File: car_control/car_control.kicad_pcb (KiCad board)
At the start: 2 copper layers, 55.9 x 76.8 mm, 21 parts, among them J1 Conn_01x02, J2 Conn_01x03, J3 Conn_01x03, Q1 IRF540N, Q2 Q_Photo_NPN, SW1 SW_SPST

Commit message: initial schematic done?
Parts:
- added H1: MountingHole, MountingHole:MountingHole_2.7mm_M2.5_DIN965_Pad, F.Cu at (135.3, 30.5)
- added H2: MountingHole, MountingHole:MountingHole_2.7mm_M2.5_DIN965_Pad, F.Cu at (184.8, 30.5)
- added H3: MountingHole, MountingHole:MountingHole_2.7mm_M2.5_DIN965_Pad, F.Cu at (184.8, 101.0)
- added H4: MountingHole, MountingHole:MountingHole_2.7mm_M2.5_DIN965_Pad, F.Cu at (135.3, 101.0)
- SW1: footprint Connector_PinHeader_2.54mm:PinHeader_1x02_P2.54mm_Vertical -> mini_slide_switch:OS102011MA1QN1
- moved J2 11.7 mm to (157.5, 38.1)
- moved D6 8.26 mm to (142.9, 100.3)
- moved R5 8.26 mm to (142.9, 94.0)
- moved D5 6.35 mm to (141.0, 30.5)
- moved R4 6.35 mm to (141.0, 35.6)
- moved J3 4.62 mm to (157.5, 31.1)
- moved SW1 0.83 mm to (134.1, 68.6), turned to -90 degrees

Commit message: working on mechanics
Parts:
- removed BT1: Battery, Connector_PinHeader_2.54mm:PinHeader_1x02_P2.54mm_Vertical
- added J4: Screw_Terminal_01x02, Connector_Wuerth:Wuerth_WR-WTB_64800211622_1x02_P1.50mm_Vertical, F.Cu at (134.6, 44.7)
- J1: value Conn_01x02 -> Screw_Terminal_01x02; footprint Connector_PinHeader_2.54mm:PinHeader_1x02_P2.54mm_Vertical -> Connector_Wuerth:Wuerth_WR-WTB_64800211622_1x02_P1.50mm_Vertical
- moved R3 56.7 mm to (144.1, 81.9)
- moved R4 46.4 mm to (138.4, 81.9)
- moved D2 28.2 mm to (146.1, 71.1)
- moved Q1 10.8 mm to (179.1, 68.6)
- moved R6 10.5 mm to (165.1, 92.1)
- moved A1 9.85 mm to (151.1, 43.2)
- moved J1 9.44 mm to (178.4, 44.6), turned to 90 degrees
- moved R1 9.03 mm to (154.9, 92.1)
- moved R2 9.03 mm to (160.0, 92.1)
- moved D3 7.73 mm to (177.8, 84.5)
- moved Q2 7.73 mm to (177.8, 89.5)
- moved R5 7.24 mm to (149.9, 92.1)
- moved H3 6.38 mm to (178.4, 100.3)
- moved D4 6.35 mm to (168.9, 30.5)
- moved D7 6.35 mm to (168.9, 100.3)
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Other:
- board size 55.9 x 76.8 mm -> 50.8 x 76.2 mm

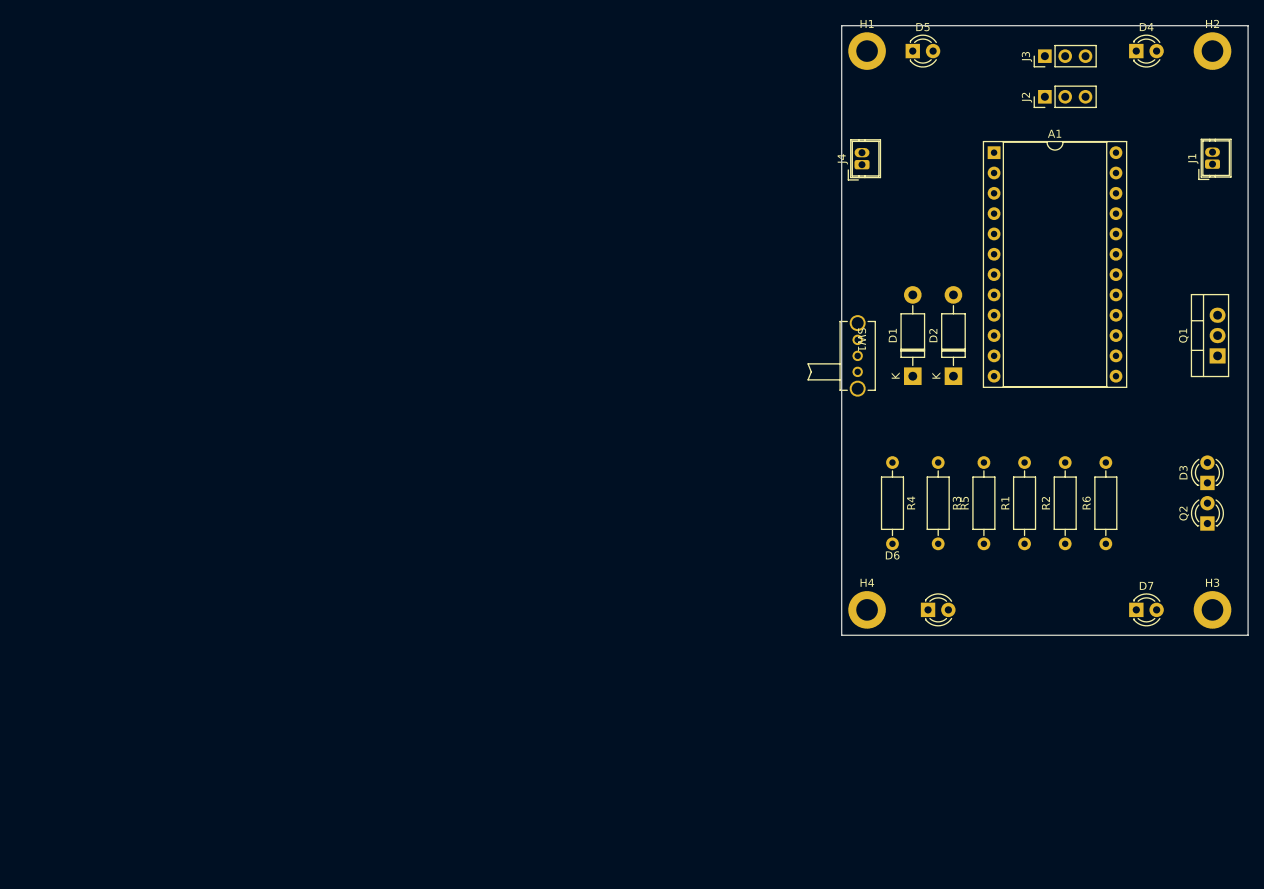
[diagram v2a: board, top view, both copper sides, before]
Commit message: New board outline with wings
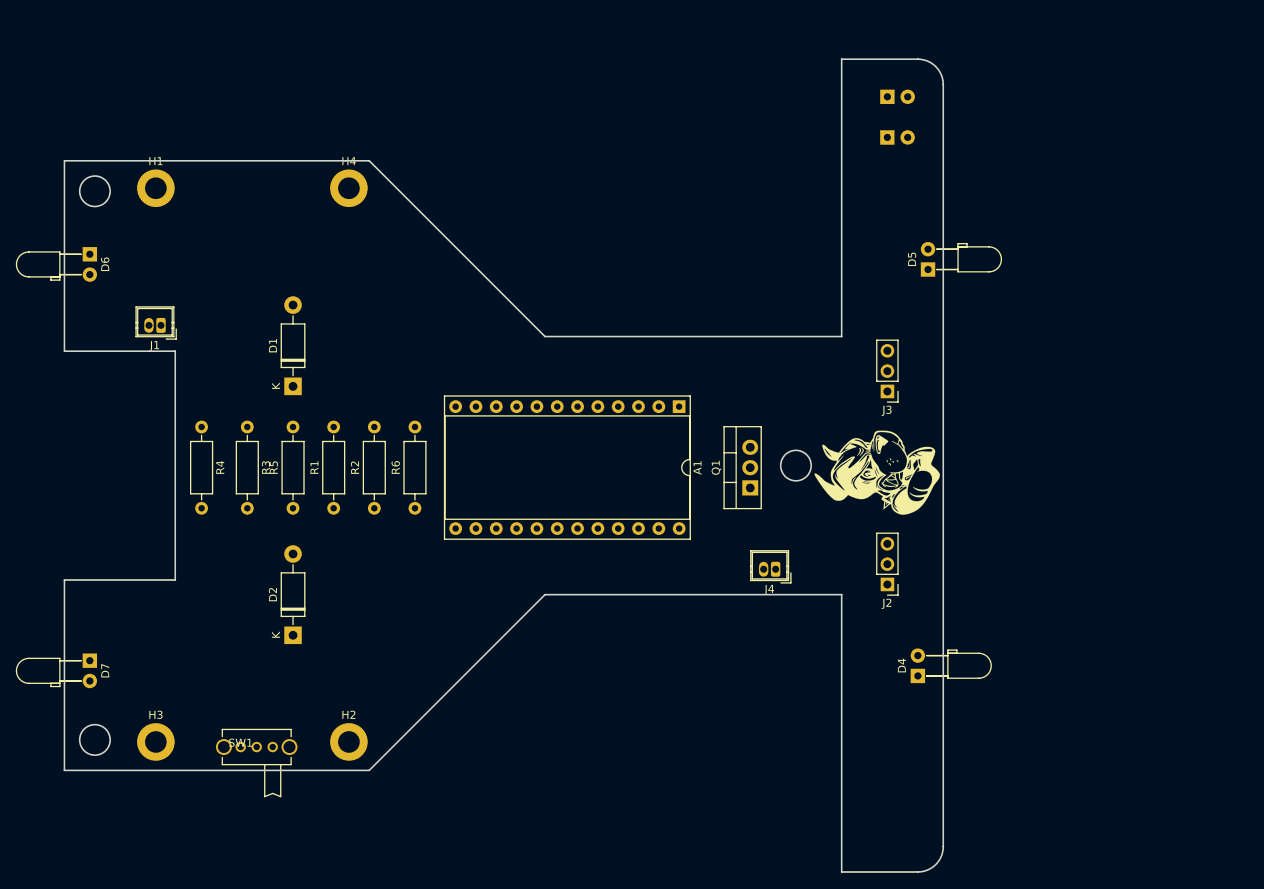
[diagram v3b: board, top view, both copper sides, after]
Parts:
- added N1: Housing, rhett_logo:rhett_logo, F.Cu at (136.5, 83.2)
- D3, Q2: moved to B.Cu
- D4, D5, D6, D7: footprint LED_THT:LED_D3.0mm_Clear -> LED_THT:LED_D3.0mm_Horizontal_O3.81mm_Z2.0mm
- moved H2 138.2 mm to (70.5, 116.8)
- moved H3 133.1 mm to (46.4, 116.8)
- moved J1 133.0 mm to (47.0, 64.8), turned to 180 degrees
- moved D7 131.0 mm to (38.1, 106.7), turned to -90 degrees
- moved D6 113.8 mm to (38.1, 55.9), turned to -90 degrees
- moved H1 90.5 mm to (46.4, 47.6)
- moved SW1 89.6 mm to (59.0, 117.5), turned to 0 degrees
- moved D2 88.7 mm to (63.5, 103.5)
- moved R2 86.5 mm to (73.7, 87.6)
- moved R3 86.5 mm to (57.8, 77.5)
- moved R4 86.5 mm to (52.1, 77.5)
- moved R5 86.5 mm to (63.5, 87.6)
- moved R1 86.5 mm to (68.6, 87.6)
- moved R6 86.5 mm to (78.7, 87.6)
- moved H4 83.5 mm to (70.5, 47.6)
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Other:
- board size 50.8 x 76.2 mm -> 109.9 x 101.6 mm

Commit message: candidate placement
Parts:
- removed D3: IR_LED, LED_THT:LED_D3.0mm_Clear
- removed Q2: Q_Photo_NPN, LED_THT:LED_D3.0mm_Clear
- added U1: TCRT5000, my_opto:TCRT5000, B.Cu at (138.4, 48.3)
- J1, J4: footprint Connector_Wuerth:Wuerth_WR-WTB_64800211622_1x02_P1.50mm_Vertical -> my_terminal:Wuerth_WR-WTB_64800211622_1x02_P1.50mm_Vertical
- Q1: footprint Package_TO_SOT_THT:TO-220-3_Vertical -> Package_TO_SOT_THT:TO-220-3_Horizontal_TabDown
- moved Q1 45.1 mm to (75.6, 86.4)
- moved R3 20.3 mm to (70.5, 93.3)
- moved R5 20.3 mm to (76.2, 103.5)
- moved R4 20.3 mm to (64.8, 93.3)
- moved R1 15.7 mm to (64.8, 72.4)
- moved R2 15.7 mm to (69.8, 72.4)
- moved R6 15.7 mm to (74.9, 72.4)
- moved J4 4.58 mm to (126.4, 91.4)
- moved D1 3.81 mm to (59.7, 72.4)
- moved D2 3.81 mm to (59.7, 103.5)
- moved A1 3.17 mm to (114.9, 74.9)
- moved J1 2.84 mm to (44.5, 63.5)
- moved D6 2.54 mm to (38.1, 53.3)
- moved D7 1.90 mm to (38.1, 108.6)
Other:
- board text added: "BATTERY"
- board text added: "BLACK"
- board text added: "MOTOR"
- board text added: "RED"

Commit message: routing
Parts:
- removed H4: MountingHole, MountingHole:MountingHole_2.7mm_M2.5_DIN965_Pad
- added D3: 1N4004, Diode_THT:D_DO-41_SOD81_P10.16mm_Horizontal, F.Cu at (65.4, 72.4)
- added LS1: Speaker, my_terminal:speaker_d12mm_h8.5_p6.5, F.Cu at (57.8, 50.8)
- added Q2: 2N3904, Package_TO_SOT_THT:TO-92_Inline, F.Cu at (86.4, 67.0)
- added R7: 470, Resistor_THT:R_Axial_DIN0207_L6.3mm_D2.5mm_P10.16mm_Horizontal, F.Cu at (70.5, 72.4)
- added SW2: SW_Push, my_pushbutton:sw_push_6.2x6.2mm_p5, F.Cu at (126.4, 73.7)
- moved U1 68.6 mm to (138.4, 116.8)
- moved H2 65.7 mm to (126.4, 82.3)
- moved R5 46.9 mm to (54.0, 62.2), turned to -90 degrees
- moved R6 39.6 mm to (54.0, 106.0)
- moved R1 33.0 mm to (65.4, 105.4)
- moved R2 33.0 mm to (70.5, 105.4)
- moved R4 32.9 mm to (75.6, 62.2)
- moved D2 31.1 mm to (59.7, 72.4)
- moved D1 23.5 mm to (59.7, 95.9), turned to -90 degrees
- moved H1 7.63 mm to (38.7, 48.0)
- moved H3 7.62 mm to (38.7, 116.6)
- moved R3 5.43 mm to (75.6, 95.2)
- moved D5 3.86 mm to (139.1, 58.4)
- moved D4 2.54 mm to (139.1, 108.6)
- moved D7 1.88 mm to (38.1, 106.7)
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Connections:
- A1 pad 14: unconnected-(A1-D16-Pad14) -> Net-(A1-D16)
- A1 pad 18: unconnected-(A1-A1-Pad18) -> Net-(A1-A1)
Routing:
- net Net-(J4-Pin_1): track 0.00 -> 86.5 mm
- net Net-(A1-D2): track 0.00 -> 67.3 mm, vias 0 -> 3
- net Net-(A1-D5): track 0.00 -> 58.7 mm, vias 0 -> 1
- net /A0: track 0.00 -> 42.9 mm, vias 0 -> 2
- net Net-(A1-A1): track 0.00 -> 36.6 mm, vias 0 -> 1
- net Net-(D1-A): track 0.00 -> 11.7 mm
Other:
- outline, holes or cut-outs redrawn

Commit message: first version done?
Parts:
- added REF**: car_as, car_as:car_as, F.Cu at (0.00, 0.00)
- A1: footprint Package_DIP:DIP-24_W15.24mm_Socket -> my_arduino:pro_micro_socket
- moved R7 10.2 mm to (70.5, 62.2), turned to -90 degrees
- moved SW2 3.81 mm to (126.4, 69.8)
- moved J4 2.54 mm to (126.4, 94.0)
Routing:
- net Net-(U1-A): track 0.00 -> 110.0 mm, vias 0 -> 1
- net Net-(A1-D7): track 0.00 -> 87.2 mm, vias 0 -> 3
- net Net-(D5-K): track 0.00 -> 82.5 mm, vias 0 -> 3
- net Net-(D4-K): track 0.00 -> 73.9 mm, vias 0 -> 1
- net Net-(A1-D6): track 0.00 -> 73.3 mm, vias 0 -> 2
- net Net-(A1-D10): track 0.00 -> 73.3 mm, vias 0 -> 3
- net Net-(A1-D4): track 0.00 -> 73.2 mm, vias 0 -> 2
- net Net-(A1-D9): track 0.00 -> 72.3 mm, vias 0 -> 2
- net /A0: track 42.9 -> 112.7 mm, vias 2 -> 4
- net Net-(D1-A): track 11.7 -> 64.7 mm, vias 0 -> 1
- net Net-(D2-K): track 0.00 -> 50.6 mm, vias 0 -> 2
- net Net-(D3-A): track 0.00 -> 43.5 mm, vias 0 -> 1
- net Net-(A1-D3): track 0.00 -> 38.3 mm, vias 0 -> 1
- net Net-(A1-D16): track 0.00 -> 36.8 mm, vias 0 -> 2
- net Net-(D6-K): track 0.00 -> 23.6 mm, vias 0 -> 1
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- added copper zone on F.Cu, net +5V
- added copper zone on B.Cu, net GND
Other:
- board text added: "Boston University"

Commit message: version 2 with tail
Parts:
- moved A1 107.6 mm to (222.4, 80.6)
- moved D1 107.6 mm to (167.1, 101.6)
- moved D2 107.6 mm to (167.1, 78.1)
- moved D3 107.6 mm to (172.8, 78.1)
- moved D4 107.6 mm to (246.5, 114.3)
- moved D5 107.6 mm to (246.5, 64.1)
- moved J2 107.6 mm to (245.2, 102.9)
- moved J3 107.6 mm to (245.2, 78.7)
- moved LS1 107.6 mm to (165.2, 56.5)
- moved Q1 107.6 mm to (183.0, 92.1)
- moved R1 107.6 mm to (172.8, 111.1)
- moved R3 107.6 mm to (183.0, 101.0)
- moved R4 107.6 mm to (183.0, 67.9)
- moved R5 107.6 mm to (161.4, 67.9)
- moved R6 107.6 mm to (161.4, 111.8)
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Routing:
- net Net-(D7-K): track 16.1 -> 85.2 mm
- net Net-(A1-D7): track 87.2 -> 156.2 mm
- net Net-(D6-K): track 23.6 -> 91.9 mm
- net Net-(A1-D6): track 73.3 -> 141.6 mm
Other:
- board size 109.9 x 101.6 mm -> 179.7 x 101.6 mm

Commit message: Add USB serial connector
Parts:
- added J5: Conn_01x06, Connector_PinHeader_2.54mm:PinHeader_1x06_P2.54mm_Vertical, F.Cu at (212.7, 76.2)
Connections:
- A1 pad 1: unconnected-(A1-D1/TX-Pad1) -> /RXI
- A1 pad 11: unconnected-(A1-D8-Pad11) -> /DTR
- A1 pad 15: unconnected-(A1-D14-Pad15) -> /CTS
- A1 pad 2: unconnected-(A1-D0/RX-Pad2) -> /TXO
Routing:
- net /CTS: track 0.00 -> 34.5 mm, vias 0 -> 2
- net /DTR: track 0.00 -> 34.5 mm, vias 0 -> 2
- net /TXO: track 0.00 -> 4.65 mm
- net /RXI: track 0.00 -> 4.65 mm
- net Net-(A1-D10): track 73.3 -> 75.0 mm
- net Net-(D5-K): track 82.5 -> 84.0 mm, vias 3 -> 5
- net Net-(A1-D5): track 60.8 -> 61.9 mm, vias 1 -> 2
